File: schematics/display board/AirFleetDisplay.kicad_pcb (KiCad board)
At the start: 2 copper layers, 99.6 x 87.1 mm, 9 parts, among them J1 Screw_Terminal_01x02, J2 Conn_01x16_Socket, J3 Conn_01x12_Socket, J4 Conn_01x16_Socket, U1 NCP1117-5.0_SOT223

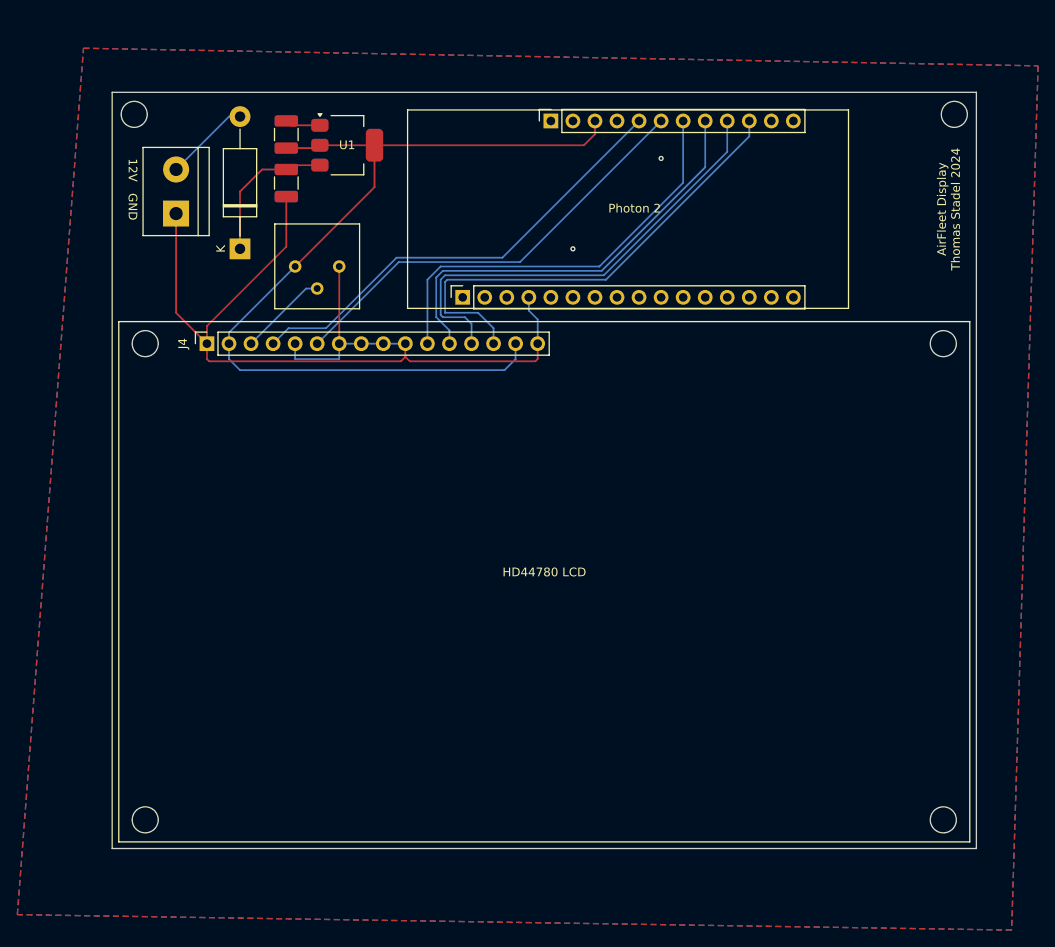
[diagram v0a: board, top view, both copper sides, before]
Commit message: Opdateret PCB til display
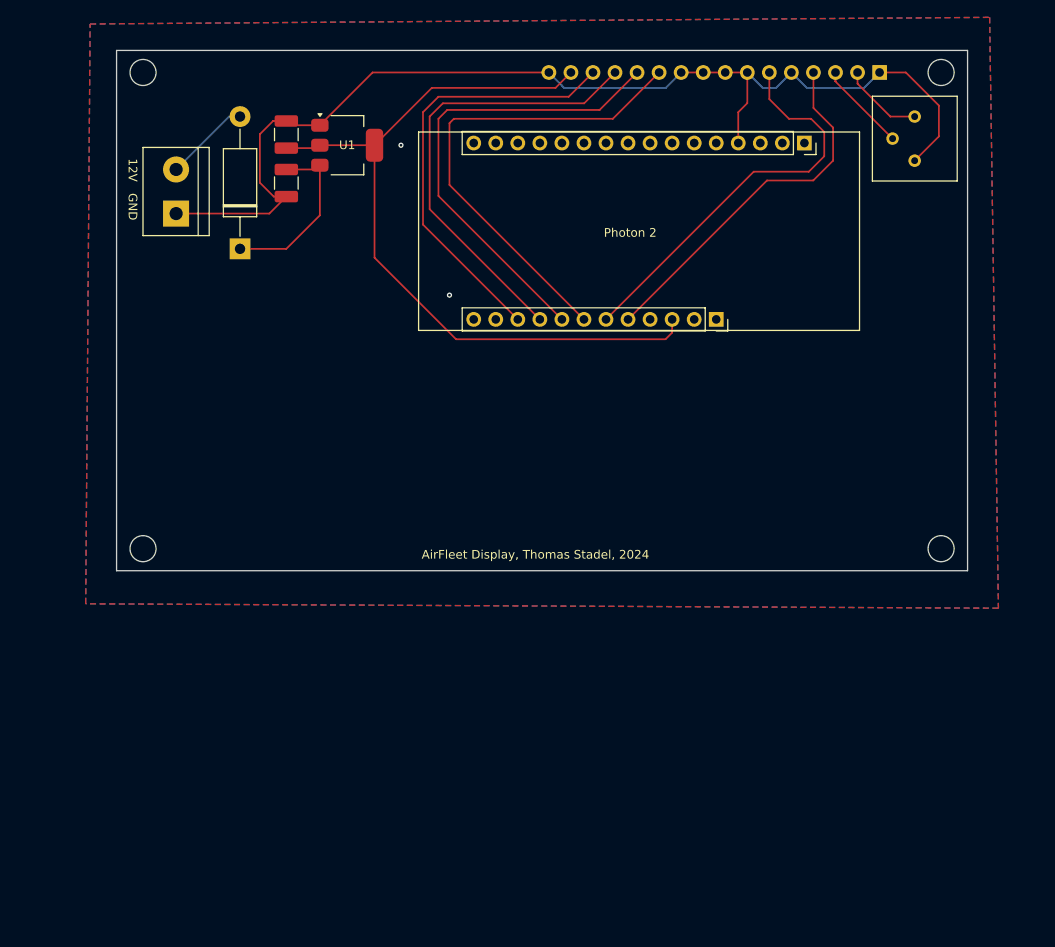
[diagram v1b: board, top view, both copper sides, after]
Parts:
- J4: moved to B.Cu
- moved J4 83.6 mm to (137.4, 58.7)
- moved RV1 73.4 mm to (141.5, 63.8), turned to 180 degrees
- moved J2 43.2 mm to (128.8, 66.8), turned to -90 degrees
- moved J3 29.8 mm to (118.6, 87.1), turned to -90 degrees
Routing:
- net GND: track 116.0 -> 126.5 mm
- net LCD_RS: track 52.8 -> 42.3 mm
- net LCD_D4: track 48.6 -> 55.6 mm
- net 5V: track 105.2 -> 98.8 mm
- net LCD_D7: track 55.4 -> 49.9 mm
- net Net-(D1-K): track 17.1 -> 21.8 mm
- net LCD_D5: track 49.8 -> 54.1 mm
- net LCD_EN: track 50.3 -> 46.7 mm
- net LCD_D6: track 53.0 -> 52.1 mm
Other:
- board size 99.6 x 87.1 mm -> 98 x 59.9 mm
- board text added: "AirFleet Display, Thomas Stadel, 2024"
- board text removed: "AirFleet Display Thomas Stadel 2024"
- board text removed: "HD44780 LCD"
